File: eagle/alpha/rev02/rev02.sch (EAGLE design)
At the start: 379 parts, among them CN1 HOST, CN2 HOST, IC1 IS45S32160F, IC2 IS45S32160F, IC3 N25Q128A13ES, IC4 N25Q128A13ES, Q1 2N7002, Q3 2N7002, Q5 ASFL1, Q6 2N7002, T1 BC847, T2 BC847, T3 BC818, U1 MC14551BDG, U2 MC74HC1G14DTT1G, U3 ATTINY828R-AU, U4 MC14551BDG, U5 23K640-I/SN, U6 MCP79412-I/SN, U7 XC7A200TFBG484, Y1 12 MHz, Y2 12 MHz

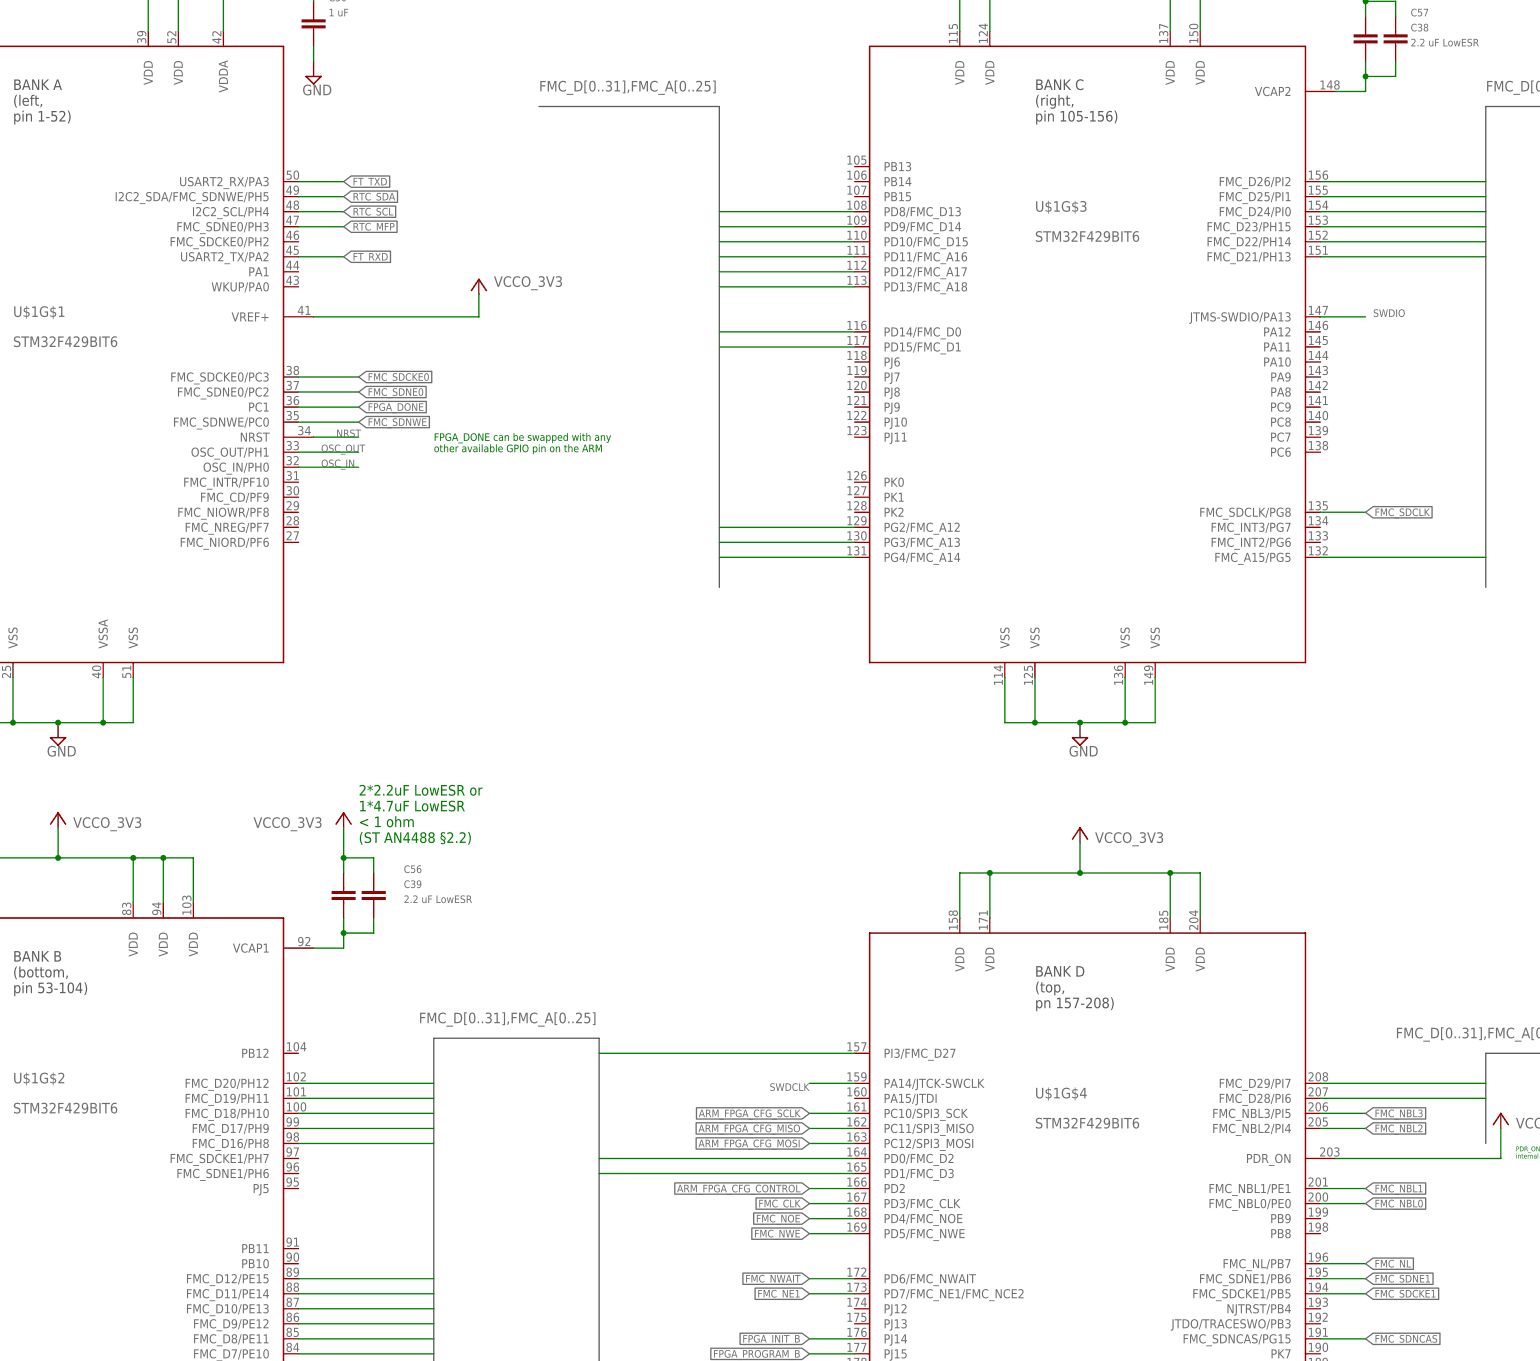
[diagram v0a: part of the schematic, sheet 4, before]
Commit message: connect ARM side of SD/MMC, MGMT USB
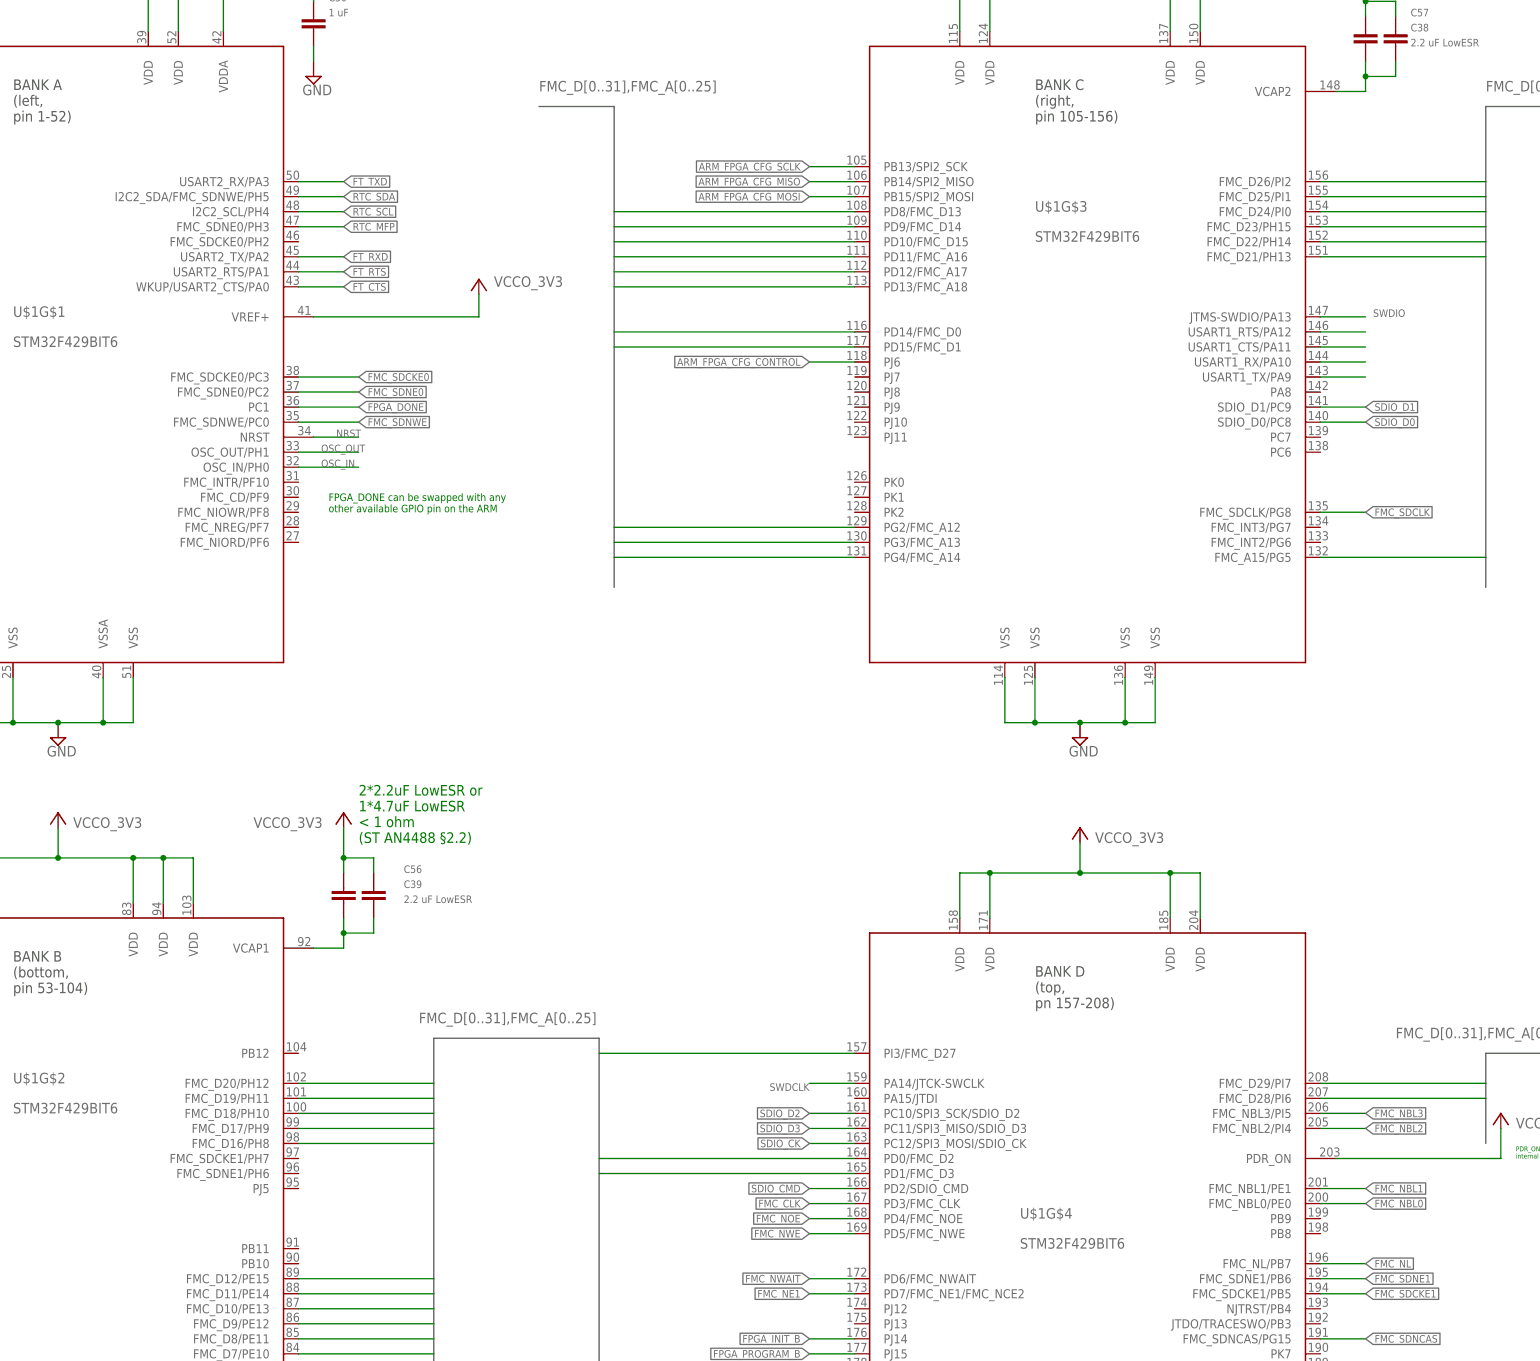
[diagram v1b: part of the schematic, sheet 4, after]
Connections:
- new net N$23: U$1G$3.USART1_TX/PA9
- new net N$25: U$1G$3.USART1_RX/PA10
- new net N$57: U$1G$3.USART1_CTS/PA11
- new net N$58: U$1G$3.USART1_RTS/PA12
- new net SDIO_CK: U$1G$4.PC12/SPI3_MOSI/SDIO_CK
- new net SDIO_CMD: U$1G$4.PD2/SDIO_CMD
- new net SDIO_D0: U$1G$3.SDIO_D0/PC8
- new net SDIO_D1: U$1G$3.SDIO_D1/PC9
- new net SDIO_D2: U$1G$4.PC10/SPI3_SCK/SDIO_D2
- new net SDIO_D3: U$1G$4.PC11/SPI3_MISO/SDIO_D3
- net ARM_FPGA_CFG_CONTROL: now also U$1G$3.PJ6; no longer U$1G$4.PD2
- net ARM_FPGA_CFG_MISO: now also U$1G$3.PB14/SPI2_MISO; no longer U$1G$4.PC11/SPI3_MISO
- net ARM_FPGA_CFG_MOSI: now also U$1G$3.PB15/SPI2_MOSI; no longer U$1G$4.PC12/SPI3_MOSI
- net ARM_FPGA_CFG_SCLK: now also U$1G$3.PB13/SPI2_SCK; no longer U$1G$4.PC10/SPI3_SCK
- net FT_CTS: now also U$1G$1.WKUP/USART2_CTS/PA0
- net FT_RTS: now also U$1G$1.USART2_RTS/PA1
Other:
- note added: "Questions: 1) Which connector to use? Haven't found good one with Eagle symbol. Some different kinds available. 2) Novena seems to have card reset capability (power control from MCU). Do we want the same? 3) Novena has two SD slots, and list power at 200mA. Do we need special power for the SD card, or can we use VCCO_3V3?"
- note added: "Should we keep this separate chip or rather connect VBAT to the STM32 and use the internal RTC?"
- note removed: "Look at Novena"

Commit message: rearrange STM32F429 symbol after functionality instead of hardware
Now that it is more known what functionality we want to use in the STM32,
it makes much more sense (and will help reviewers a great deal) to have
the symbol in the schematics arranged after used functionality rather than
after how the hardware pinout is.
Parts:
- C38, C39, C56, C57: value 2.2 uF LowESR -> 2.2 uF
- U$1: device STM32F429:STM32F429BIT6 -> Alpha-IC:STM32F429BIT6
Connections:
- removed net N$23: U$1G$3.USART1_TX/PA9
- removed net N$25: U$1G$3.USART1_RX/PA10
- removed net N$57: U$1G$3.USART1_CTS/PA11
- removed net N$58: U$1G$3.USART1_RTS/PA12
- net ARM_FPGA_CFG_CONTROL: now also U$1IO.PJ6; no longer U$1G$3.PJ6
- net ARM_FPGA_CFG_MISO: now also U$1IO.SPI2_MISO/PB14; no longer U$1G$3.PB14/SPI2_MISO
- net ARM_FPGA_CFG_MOSI: now also U$1IO.SPI2_MOSI/PB15; no longer U$1G$3.PB15/SPI2_MOSI
- net ARM_FPGA_CFG_SCLK: now also U$1IO.SPI2_SCK/PB13; no longer U$1G$3.PB13/SPI2_SCK
- net ARM_LED1: now also U$1IO.PJ4; no longer U$1G$2.PJ4
- net ARM_LED2: now also U$1IO.PJ3; no longer U$1G$2.PJ3
- net ARM_LED3: now also U$1IO.PJ2; no longer U$1G$2.PJ2
- net ARM_LED4: now also U$1IO.PJ1; no longer U$1G$2.PJ1
- net AVR_GPIO_10: now also U$1IO.PC13; no longer U$1G$1.PC13
- net AVR_GPIO_11: no longer U$1G$1.PI11
- net BOOT0: now also U$1CFG.BOOT0@197; no longer U$1G$4.BOOT0@197
- net FMC_A0: now also U$1FMC.FMC_A0/PF0; no longer U$1G$1.PF0/FMC_A0
- net FMC_A1: now also U$1FMC.FMC_A1/PF1; no longer U$1G$1.PF1/FMC_A1
- net FMC_A10: now also U$1FMC.FMC_A10/PG0; no longer U$1G$2.PG0/FMC_A10
- net FMC_A11: now also U$1FMC.FMC_A11/PG1; no longer U$1G$2.PG1/FMC_A11
- net FMC_A12: now also U$1FMC.FMC_A12/PG2; no longer U$1G$3.PG2/FMC_A12
- net FMC_A13: now also U$1FMC.FMC_A13/PG3; no longer U$1G$3.PG3/FMC_A13
- net FMC_A14: now also U$1FMC.FMC_A14/PG4; no longer U$1G$3.PG4/FMC_A14
- net FMC_A15: now also U$1FMC.FMC_A15/PG5; no longer U$1G$3.FMC_A15/PG5
- net FMC_A16: now also U$1FMC.FMC_A16/PD11; no longer U$1G$3.PD11/FMC_A16
- net FMC_A17: now also U$1FMC.FMC_A17/PD12; no longer U$1G$3.PD12/FMC_A17
- net FMC_A18: now also U$1FMC.FMC_A18/PD13; no longer U$1G$3.PD13/FMC_A18
- net FMC_A19: now also U$1FMC.FMC_A19/PE3; no longer U$1G$1.PE3/FMC_A19
- net FMC_A2: now also U$1FMC.FMC_A2/PF2; no longer U$1G$1.PF2/FMC_A2
- net FMC_A20: now also U$1FMC.FMC_A20/PE4; no longer U$1G$1.PE4/FMC_A20
- net FMC_A21: now also U$1FMC.FMC_A21/PE5; no longer U$1G$1.PE5/FMC_A21
- net FMC_A22: now also U$1FMC.FMC_A22/PE6; no longer U$1G$1.PE6/FMC_A22
- net FMC_A23: now also U$1FMC.FMC_A23/PE2; no longer U$1G$1.PE2/FMC_A23
- net FMC_A24: now also U$1FMC.FMC_A24/PG13; no longer U$1G$4.PG13/FMC_A24
- net FMC_A25: now also U$1FMC.FMC_A25/PG14; no longer U$1G$4.PG14/FMC_A25
- net FMC_A3: now also U$1FMC.FMC_A3/PF3; no longer U$1G$1.PF3/FMC_A3
- net FMC_A4: now also U$1FMC.FMC_A4/PF4; no longer U$1G$1.PF4/FMC_A4
- net FMC_A5: now also U$1FMC.FMC_A5/PF5; no longer U$1G$1.PF5/FMC_A5
- net FMC_A6: now also U$1FMC.FMC_A6/PF12; no longer U$1G$2.PF12/FMC_A6
- net FMC_A7: now also U$1FMC.FMC_A7/PF13; no longer U$1G$2.PF13/FMC_A7
- net FMC_A8: now also U$1FMC.FMC_A8/PF14; no longer U$1G$2.PF14/FMC_A8
- net FMC_A9: now also U$1FMC.FMC_A9/PF15; no longer U$1G$2.PF15/FMC_A9
- net FMC_CLK: now also U$1FMC.FMC_CLK/PD3; no longer U$1G$4.PD3/FMC_CLK
- net FMC_D0: now also U$1FMC.PD14/FMC_D0; no longer U$1G$3.PD14/FMC_D0
- net FMC_D1: now also U$1FMC.PD15/FMC_D1; no longer U$1G$3.PD15/FMC_D1
- net FMC_D10: now also U$1FMC.PE13/FMC_D10; no longer U$1G$2.FMC_D10/PE13
- net FMC_D11: now also U$1FMC.PE14/FMC_D11; no longer U$1G$2.FMC_D11/PE14
- net FMC_D12: now also U$1FMC.PE15/FMC_D12; no longer U$1G$2.FMC_D12/PE15
- net FMC_D13: now also U$1FMC.PD8/FMC_D13; no longer U$1G$3.PD8/FMC_D13
- net FMC_D14: now also U$1FMC.PD9/FMC_D14; no longer U$1G$3.PD9/FMC_D14
- net FMC_D15: now also U$1FMC.PD10/FMC_D15; no longer U$1G$3.PD10/FMC_D15
- net FMC_D16: now also U$1FMC.PH8/FMC_D16; no longer U$1G$2.FMC_D16/PH8
- net FMC_D17: now also U$1FMC.PH9/FMC_D17; no longer U$1G$2.FMC_D17/PH9
- net FMC_D18: now also U$1FMC.PH10/FMC_D18; no longer U$1G$2.FMC_D18/PH10
- net FMC_D19: now also U$1FMC.PH11/FMC_D19; no longer U$1G$2.FMC_D19/PH11
- net FMC_D2: now also U$1FMC.PD0/FMC_D2; no longer U$1G$4.PD0/FMC_D2
- net FMC_D20: now also U$1FMC.PH12/FMC_D20; no longer U$1G$2.FMC_D20/PH12
- net FMC_D21: now also U$1FMC.PH13/FMC_D21; no longer U$1G$3.FMC_D21/PH13
- net FMC_D22: now also U$1FMC.PH14/FMC_D22; no longer U$1G$3.FMC_D22/PH14
- net FMC_D23: now also U$1FMC.PH15/FMC_D23; no longer U$1G$3.FMC_D23/PH15
- net FMC_D24: now also U$1FMC.PI0/FMC_D24; no longer U$1G$3.FMC_D24/PI0
- net FMC_D25: now also U$1FMC.PI1/FMC_D25; no longer U$1G$3.FMC_D25/PI1
- net FMC_D26: now also U$1FMC.PI2/FMC_D26; no longer U$1G$3.FMC_D26/PI2
- net FMC_D27: now also U$1FMC.PI3/FMC_D27; no longer U$1G$4.PI3/FMC_D27
- net FMC_D28: now also U$1FMC.PI6/FMC_D28; no longer U$1G$4.FMC_D28/PI6
- net FMC_D29: now also U$1FMC.PI7/FMC_D29; no longer U$1G$4.FMC_D29/PI7
- net FMC_D3: now also U$1FMC.PD1/FMC_D3; no longer U$1G$4.PD1/FMC_D3
- net FMC_D30: now also U$1FMC.PI9/FMC_D30; no longer U$1G$1.PI9/FMC_D30
- net FMC_D31: now also U$1FMC.PI10/FMC_D31; no longer U$1G$1.PI10/FMC_D31
- net FMC_D4: now also U$1FMC.PE7/FMC_D4; no longer U$1G$2.PE7/FMC_D4
- net FMC_D5: now also U$1FMC.PE8/FMC_D5; no longer U$1G$2.FMC_D5/PE8
- net FMC_D6: now also U$1FMC.PE9/FMC_D6; no longer U$1G$2.FMC_D6/PE9
- net FMC_D7: now also U$1FMC.PE10/FMC_D7; no longer U$1G$2.FMC_D7/PE10
- net FMC_D8: now also U$1FMC.PE11/FMC_D8; no longer U$1G$2.FMC_D8/PE11
- net FMC_D9: now also U$1FMC.PE12/FMC_D9; no longer U$1G$2.FMC_D9/PE12
- net FMC_NBL0: now also U$1FMC.FMC_NBL0/PE0; no longer U$1G$4.FMC_NBL0/PE0
- net FMC_NBL1: now also U$1FMC.FMC_NBL1/PE1; no longer U$1G$4.FMC_NBL1/PE1
- net FMC_NBL2: now also U$1FMC.FMC_NBL2/PI4; no longer U$1G$4.FMC_NBL2/PI4
- net FMC_NBL3: now also U$1FMC.FMC_NBL3/PI5; no longer U$1G$4.FMC_NBL3/PI5
- net FMC_NE1: now also U$1FMC.FMC_NE1/PD7; no longer U$1G$4.PD7/FMC_NE1/FMC_NCE2
- net FMC_NL: now also U$1FMC.FMC_NL/PB7; no longer U$1G$4.FMC_NL/PB7
- net FMC_NOE: now also U$1FMC.FMC_NOE/PD4; no longer U$1G$4.PD4/FMC_NOE
- net FMC_NWAIT: now also U$1FMC.FMC_NWAIT/PD6; no longer U$1G$4.PD6/FMC_NWAIT
- net FMC_NWE: now also U$1FMC.FMC_NWE/PD5; no longer U$1G$4.PD5/FMC_NWE
- net FMC_SDCKE0: now also U$1FMC.PC3/FMC_SDCKE0; no longer U$1G$1.FMC_SDCKE0/PC3
- net FMC_SDCKE1: now also U$1FMC.PB5/FMC_SDCKE1; no longer U$1G$4.FMC_SDCKE1/PB5
- net FMC_SDCLK: now also U$1FMC.PG8/FMC_SDCLK; no longer U$1G$3.FMC_SDCLK/PG8
- net FMC_SDNCAS: now also U$1FMC.PG15/FMC_SDNCAS; no longer U$1G$4.FMC_SDNCAS/PG15
- net FMC_SDNE0: now also U$1FMC.PC2/FMC_SDNE0; no longer U$1G$1.FMC_SDNE0/PC2
- net FMC_SDNE1: now also U$1FMC.PB6/FMC_SDNE1; no longer U$1G$4.FMC_SDNE1/PB6
- net FMC_SDNRAS: now also U$1FMC.PF11/FMC_SDNRAS; no longer U$1G$2.PF11/FMC_SDNRAS
- net FMC_SDNWE: now also U$1FMC.PC0/FMC_SDNWE; no longer U$1G$1.FMC_SDNWE/PC0
- net FPGA_DONE: now also U$1IO.PJ7; no longer U$1G$1.PC1
- net FPGA_INIT_B: now also U$1IO.PJ14; no longer U$1G$4.PJ14
- net FPGA_IRQ_N_0: now also U$1IO.PJ13; no longer U$1G$4.PG12/FMC_NE4
- net FPGA_IRQ_N_1: now also U$1IO.PJ12; no longer U$1G$4.PG11/FMC_NCE4_2
- net FPGA_IRQ_N_2: now also U$1IO.PJ11; no longer U$1G$4.PG10/FMC_NCE4_1/FMC_NE3
- net FPGA_IRQ_N_3: now also U$1IO.PJ10; no longer U$1G$4.PG9/FMC_NE2/FMC_NCE3
- net FPGA_PROGRAM_B: now also U$1IO.PJ15; no longer U$1G$4.PJ15
- net FT_CTS: now also U$1IO.USART2_CTS/WKUP/PA0; no longer U$1G$1.WKUP/USART2_CTS/PA0
- net FT_MGMT_CTS: now also U$1IO.USART1_CTS/PA11
- net FT_MGMT_RTS: now also U$1IO.USART1_RTS/PA12
- net FT_MGMT_RXD: now also U$1IO.USART1_TX/PA9
- net FT_MGMT_TXD: now also U$1IO.USART1_RX/PA10
- net FT_RTS: now also U$1IO.USART2_RTS/PA1; no longer U$1G$1.USART2_RTS/PA1
- net FT_RXD: now also U$1IO.USART2_TX/PA2; no longer U$1G$1.USART2_TX/PA2
- net FT_TXD: now also U$1IO.USART2_RX/PA3; no longer U$1G$1.USART2_RX/PA3
- net GND: now also U$1PWR.VSS@114, U$1PWR.VSS@125, U$1PWR.VSS@136, U$1PWR.VSS@14, U$1PWR.VSS@149, U$1PWR.VSS@170, U$1PWR.VSS@184, U$1PWR.VSS@202, U$1PWR.VSS@25, U$1PWR.VSS@51, U$1PWR.VSS@60, U$1PWR.VSS@72, U$1PWR.VSS@82, U$1PWR.VSS@93, U$1PWR.VSSA@40; no longer U$1G$1.VSS@14, U$1G$1.VSS@25, U$1G$1.VSS@51, U$1G$1.VSSA@40, U$1G$2.VSS@60, U$1G$2.VSS@72, U$1G$2.VSS@82, U$1G$2.VSS@93, U$1G$3.VSS@114, U$1G$3.VSS@125, U$1G$3.VSS@136, U$1G$3.VSS@149, U$1G$4.VSS@170, U$1G$4.VSS@184, U$1G$4.VSS@202
- net KSM_PROM_MISO: now also U$1IO.SPI1_MISO/PA6; no longer U$1G$2.PA6/SPI1_MISO
- net KSM_PROM_MOSI: now also U$1IO.SPI1_MOSI/PA7; no longer U$1G$2.PA7/SPI1_MOSI
- net KSM_PROM_SCLK: now also U$1IO.SPI1_SCK/PA5; no longer U$1G$2.PA5/SPI1_SCK
- net NRST: now also U$1CFG.NRST; no longer U$1G$1.NRST@34
- net OSC_IN: now also U$1CFG.OSC_IN/PH0; no longer U$1G$1.OSC_IN/PH0
- net OSC_OUT: now also U$1CFG.OSC_OUT/PH1; no longer U$1G$1.OSC_OUT/PH1
- net RTC_MFP: now also U$1IO.PH3/FMC_SDNE0; no longer U$1G$1.FMC_SDNE0/PH3
- net RTC_SCL: now also U$1IO.I2C2_SCL/PH4; no longer U$1G$1.I2C2_SCL/PH4
- net RTC_SDA: now also U$1IO.I2C2_SDA/FMC_SDNWE/PH5; no longer U$1G$1.I2C2_SDA/FMC_SDNWE/PH5
- net SDIO_CK: now also U$1IO.SDIO_CK/SPI3_MOSI/PC12; no longer U$1G$4.PC12/SPI3_MOSI/SDIO_CK
- net SDIO_CMD: now also U$1IO.SDIO_CMD/PD2; no longer U$1G$4.PD2/SDIO_CMD
- net SDIO_D0: now also U$1IO.SDIO_D0/PC8; no longer U$1G$3.SDIO_D0/PC8
- net SDIO_D1: now also U$1IO.SDIO_D1/PC9; no longer U$1G$3.SDIO_D1/PC9
- net SDIO_D2: now also U$1IO.SDIO_D2/SPI3_SCK/PC10; no longer U$1G$4.PC10/SPI3_SCK/SDIO_D2
- net SDIO_D3: now also U$1IO.SDIO_D3/SPI3_MISO/PC11; no longer U$1G$4.PC11/SPI3_MISO/SDIO_D3
- net SWDCLK: now also U$1CFG.PA14/JTCK-SWCLK; no longer U$1G$4.PA14/JTCK-SWCLK
- net SWDIO: now also U$1CFG.PA13/JTMS-SWDIO; no longer U$1G$3.JTMS-SWDIO/PA13
- net VCAP1: now also U$1PWR.VCAP1@92; no longer U$1G$2.VCAP1@92
- net VCAP2: now also U$1PWR.VCAP2@148; no longer U$1G$3.VCAP2@148
- net VCCO_3V3: now also U$1CFG.PDR_ON@203, U$1CFG.VREF+@41, U$1PWR.VBAT@6, U$1PWR.VDD@103, U$1PWR.VDD@115, U$1PWR.VDD@124, U$1PWR.VDD@137, U$1PWR.VDD@15, U$1PWR.VDD@150, U$1PWR.VDD@158, U$1PWR.VDD@171, U$1PWR.VDD@185, U$1PWR.VDD@204, U$1PWR.VDD@26, U$1PWR.VDD@39, U$1PWR.VDD@52, U$1PWR.VDD@59, U$1PWR.VDD@73, U$1PWR.VDD@83, U$1PWR.VDD@94, U$1PWR.VDDA@42; no longer U$1G$1.VBAT@6, U$1G$1.VDD@15, U$1G$1.VDD@26, U$1G$1.VDD@39, U$1G$1.VDD@52, U$1G$1.VDDA@42, U$1G$1.VREF+@41, U$1G$2.VDD@103, U$1G$2.VDD@59, U$1G$2.VDD@73, U$1G$2.VDD@83, U$1G$2.VDD@94, U$1G$3.VDD@115, U$1G$3.VDD@124, U$1G$3.VDD@137, U$1G$3.VDD@150, U$1G$4.PDR_ON@203, U$1G$4.VDD@158, U$1G$4.VDD@171, U$1G$4.VDD@185, U$1G$4.VDD@204
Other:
- note added: "2*2*2.2uF LowESR or 2*1*4.7uF LowESR < 1 ohm (ST AN4488 §2.2)"
- note added: "Basic configuration, STM32"
- note added: "Input/output, STM32"
- note added: "Power and bypass capacitors, STM32"
- note added: "Questions: 1) Which connector to use? Haven't found a good one with Eagle symbol. Some different kinds available. 2) Novena seems to have card reset capability (power control from MCU). Do we want the same? 3) Novena has two SD slots, and list power at 200mA. Do we need a separate power regulator for the SD card, or can we use VCCO_3V3?"
- note added: "XXX cross RTS/CTS?"
- note removed: "2*2.2uF LowESR or 1*4.7uF LowESR < 1 ohm (ST AN4488 §2.2)"
- note removed: "Questions: 1) Which connector to use? Haven't found good one with Eagle symbol. Some different kinds available. 2) Novena seems to have card reset capability (power control from MCU). Do we want the same? 3) Novena has two SD slots, and list power at 200mA. Do we need special power for the SD card, or can we use VCCO_3V3?"
